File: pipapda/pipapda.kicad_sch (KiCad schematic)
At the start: 116 parts, among them U2 STM32F103RGTx

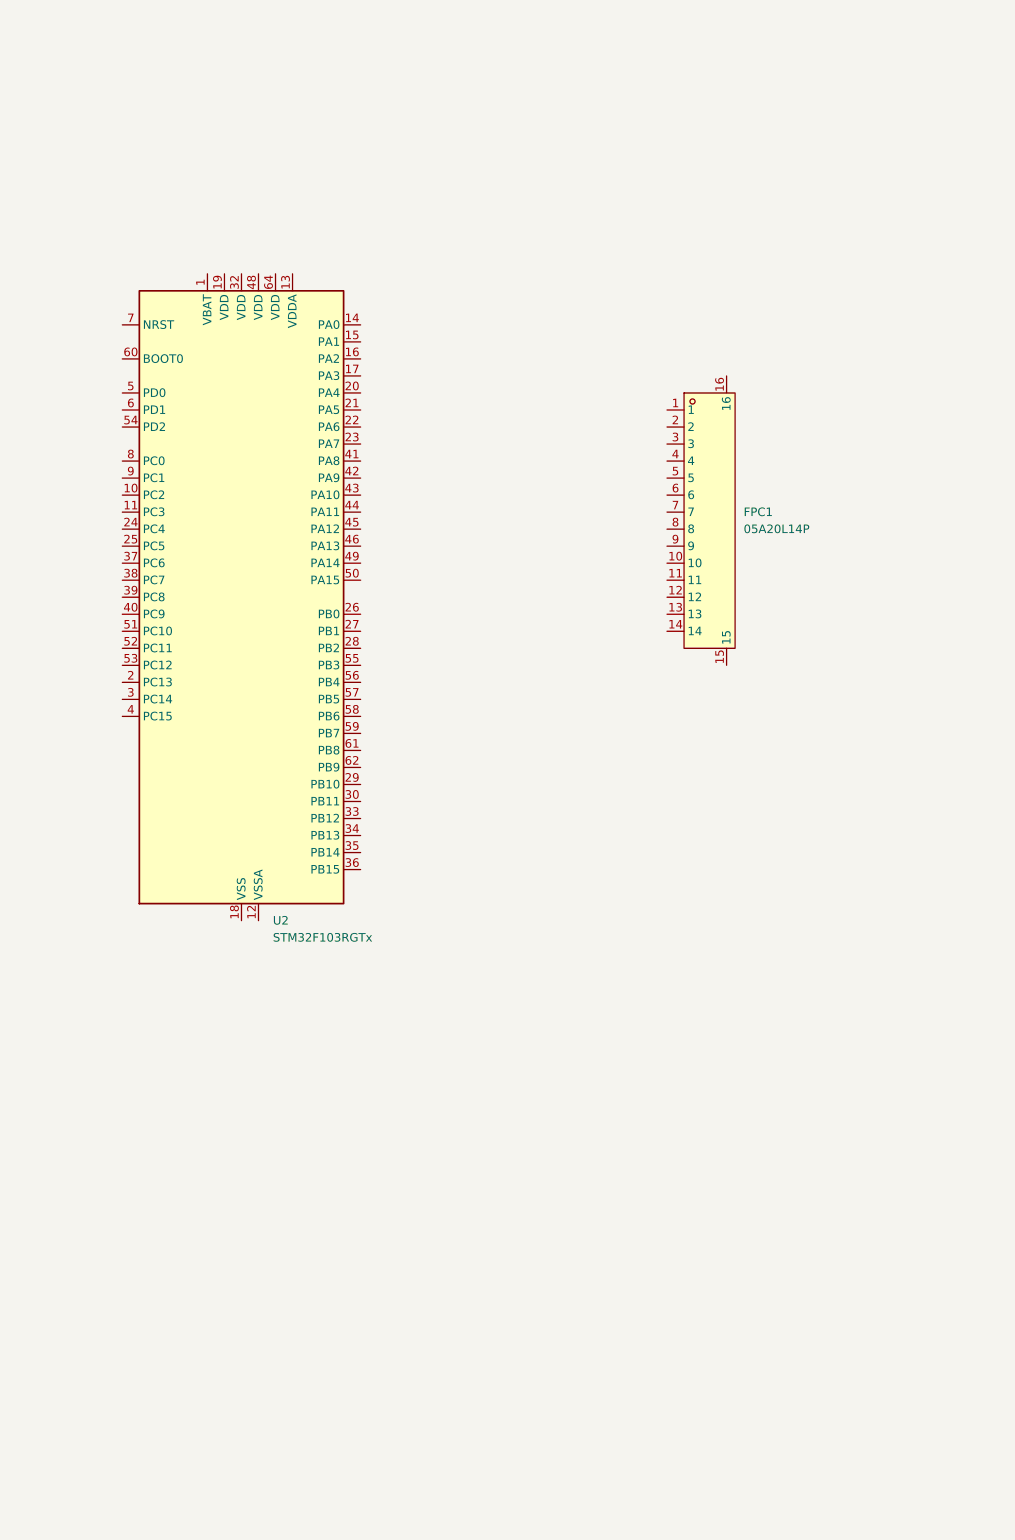
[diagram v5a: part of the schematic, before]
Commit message: add decouplers and switches for boot0 and nrst
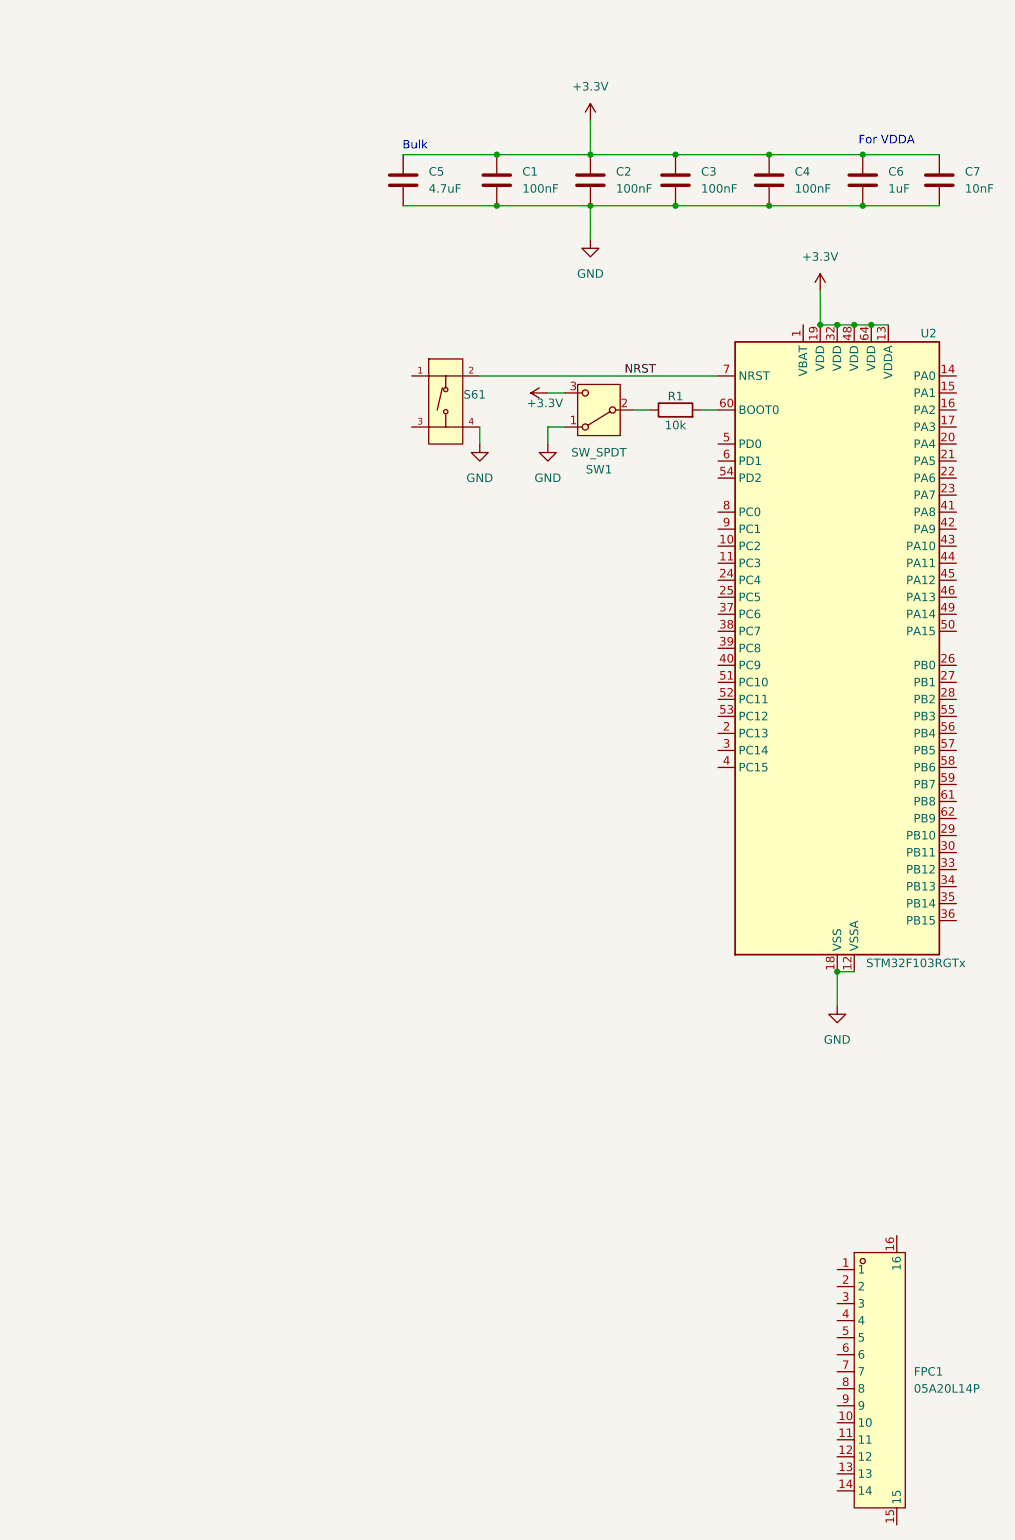
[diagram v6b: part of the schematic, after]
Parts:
- added C1, C2, C3, C4: 100nF, symbol Device:C
- added C5: 4.7uF, symbol Device:C
- added C6: 1uF, symbol Device:C
- added C7: 10nF, symbol Device:C
- added R1: 10k, symbol Device:R
- added S61: Tactile Button, 160gf, easyeda2kicad:SW-SMD_4P-L5.1-W5.1-P3.70-LS6.5-TL_H1.5, symbol PCM_JLCPCB-Connectors_Buttons:Tactile Button, 160gf, 12V, 50mA, 5.1mm
- added SW1: SW_SPDT, symbol Switch:SW_SPDT
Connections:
- net GND: now reaches U2.12 (VSSA)
- net GND: now also U2.18 (VSS), U2.31 (VSS), U2.47 (VSS), U2.63 (VSS), C1.2, C2.2, C3.2, C4.2, C5.2, C6.2, C7.2, S61.4 (D), SW1.1 (A)
- net +3.3V: now reaches U2.13 (VDDA)
- net +3.3V: now also U2.19 (VDD), U2.32 (VDD), U2.48 (VDD), U2.64 (VDD), C1.1, C2.1, C3.1, C4.1, C5.1, C6.1, C7.1, SW1.3 (C)
- net at U2.60 (BOOT0): now also R1.2
- net NRST: now reaches U2.7 (NRST)
- net NRST: now also S61.2 (B)
- new net: R1.1, SW1.2 (B)
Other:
- note added: "Bulk"
- note added: "For VDDA"
- moved on the sheet: FPC1, U2
